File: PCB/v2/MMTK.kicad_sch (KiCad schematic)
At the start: 9 parts

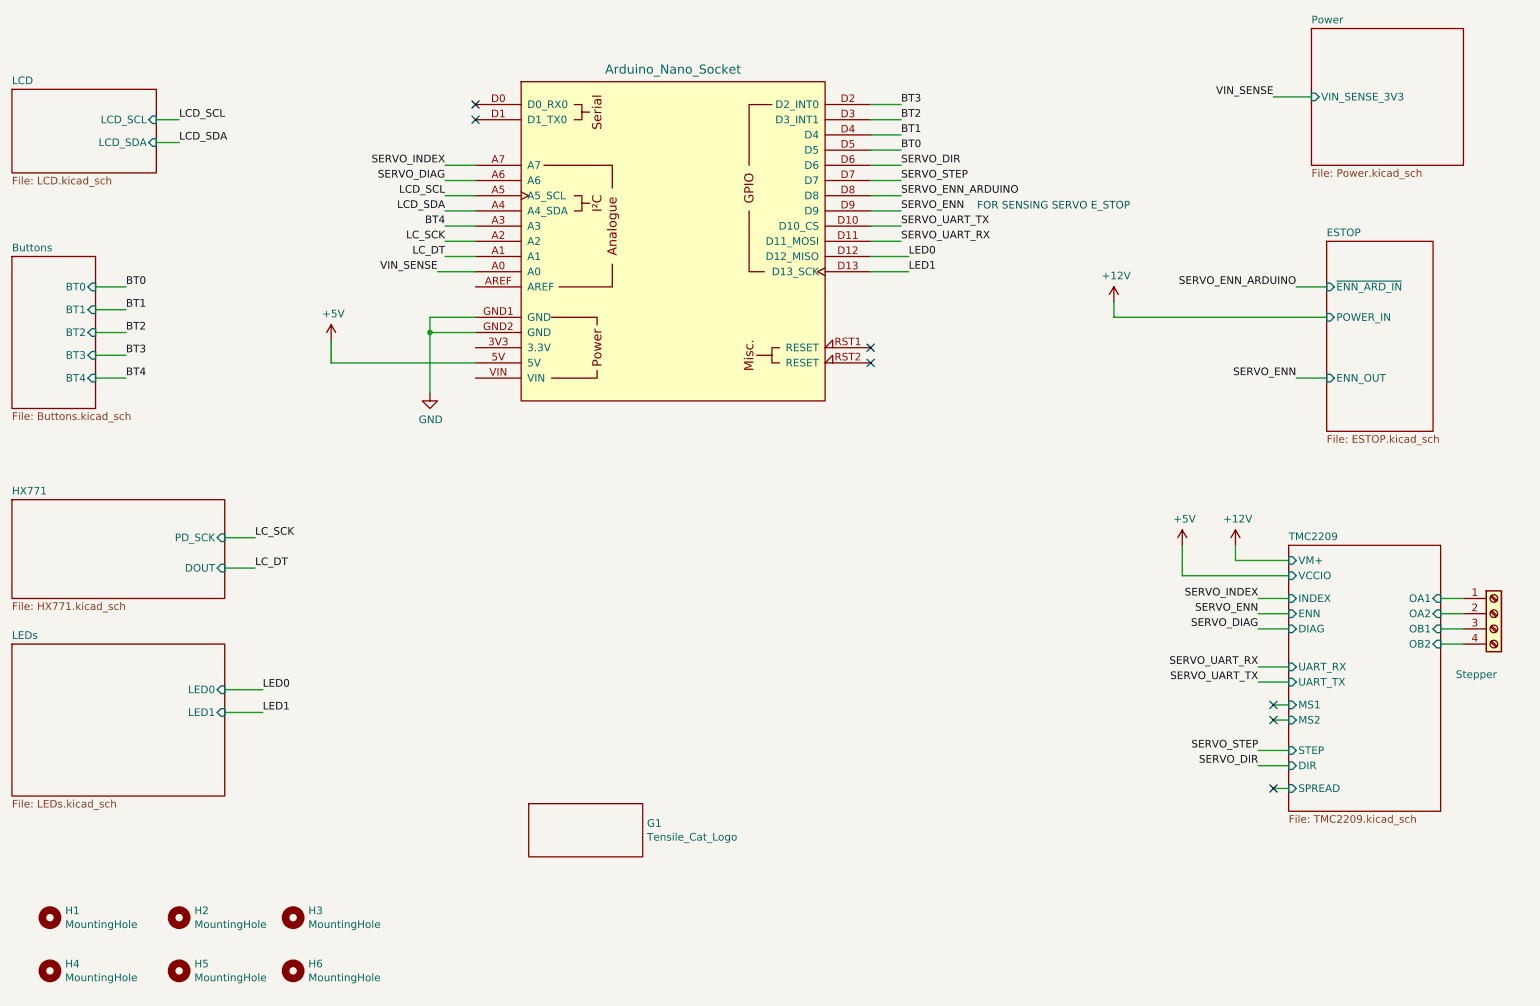
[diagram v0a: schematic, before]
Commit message: WIP updated symbols for tmc5106
Updated footprint for tmc5106,
need to check how motor wiring is done, might be wired up stupid before and that's gonna be sad
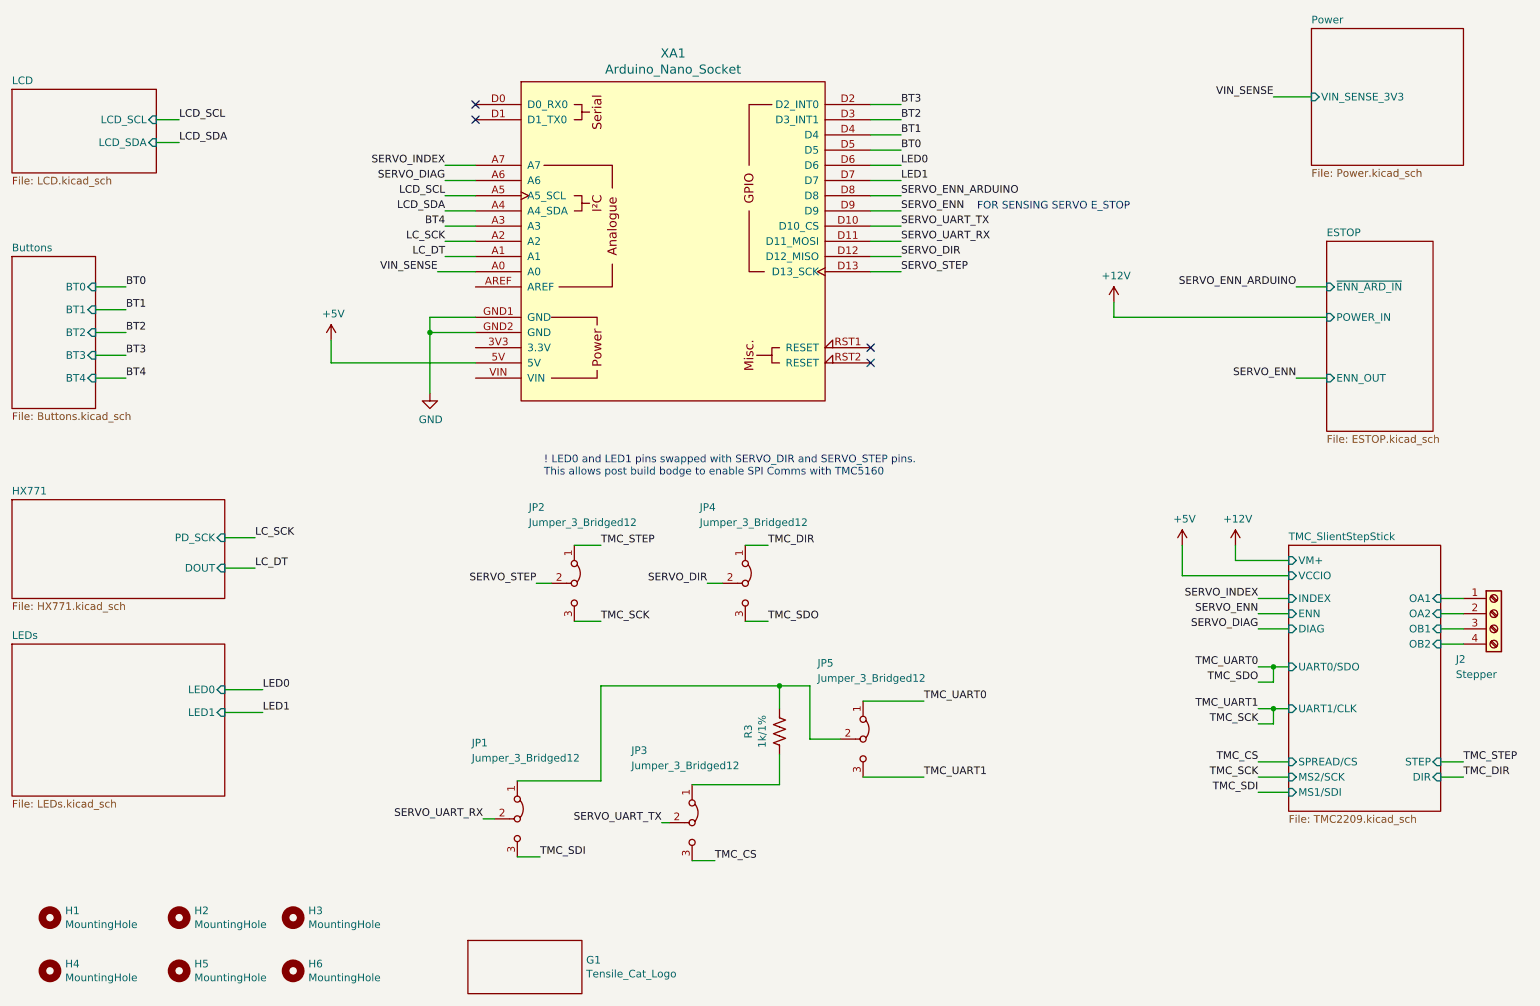
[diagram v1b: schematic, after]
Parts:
- added JP1, JP2, JP3, JP4, JP5: Jumper_3_Bridged12, Jumper:SolderJumper-3_P1.3mm_Bridged12_Pad1.0x1.5mm_NumberLabels, symbol Jumper:Jumper_3_Bridged12
- added R3: 1k/1%, Resistor_SMD:R_0603_1608Metric, symbol MMTK-rescue:R_US-Device-MMTK-rescue-MMTK-rescue
- gave numbers to parts that had none: 2
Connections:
- net LED0: now also XA1.D6; no longer XA1.D12 (D12_MISO)
- net LED1: now also XA1.D7; no longer XA1.D13 (D13_SCK)
- net SERVO_DIR: now also XA1.D12 (D12_MISO), JP4.2 (C); no longer XA1.D6
- net SERVO_STEP: now also XA1.D13 (D13_SCK), JP2.2 (C); no longer XA1.D7
- net SERVO_UART_RX: now also JP1.2 (C)
- net SERVO_UART_TX: now also JP3.2 (C)
- new net: JP1.1 (A), JP5.2 (C), R3.1
- new net: JP3.1 (A), R3.2
- new net TMC_CS: JP3.3 (B)
- new net TMC_DIR: JP4.1 (A)
- new net TMC_SCK: JP2.3 (B), JP5.3 (B)
- new net TMC_SDI: JP1.3 (B)
- new net TMC_SDO: JP4.3 (B), JP5.1 (A)
- new net TMC_STEP: JP2.1 (A)
- no-connect marks 7 -> 4
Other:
- sheet TMC2209 renamed TMC_SlientStepStick
- sheet TMC_SlientStepStick ports: added MS1/SDI, MS2/SCK, SPREAD/CS, UART0/SDO, UART1/CLK; removed MS1, MS2, SPREAD, UART_RX, UART_TX
- note added: "! LED0 and LED1 pins swapped with SERVO_DIR and SERVO_STEP pins. This allows post build bodge to enable SPI Comms with TMC5160"
- moved on the sheet: G1

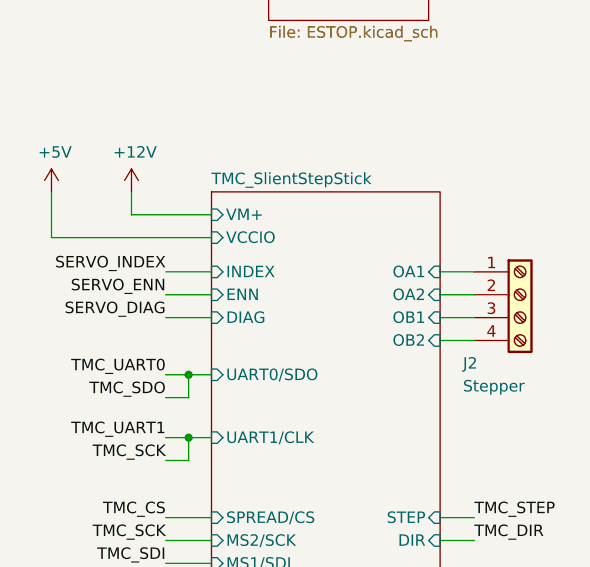
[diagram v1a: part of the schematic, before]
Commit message: Figured Out Motor Wiring
Updated motor wiring, naming on slient step stick is the same as tmc chips itself.
Phrases are A and B and 1/2 are the wires from the same phrase.
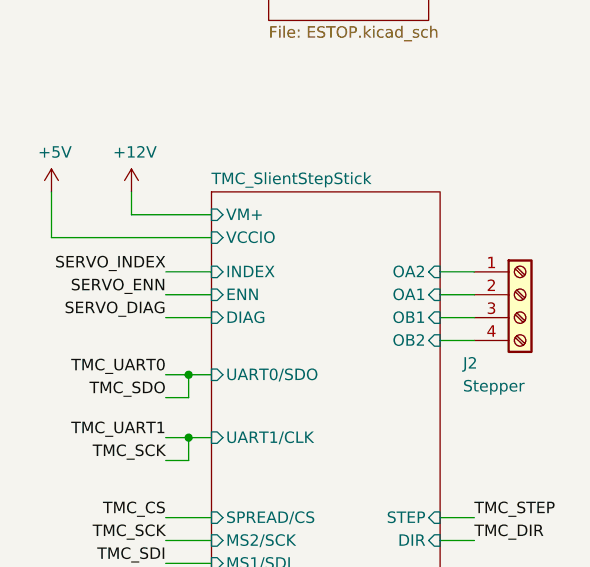
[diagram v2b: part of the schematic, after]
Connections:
- net TMC_SlientStepStick/OA1: now also J2.2 (Pin_2); no longer J2.1 (Pin_1)
- net TMC_SlientStepStick/OA2: now also J2.1 (Pin_1); no longer J2.2 (Pin_2)
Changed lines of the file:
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@@
       (effects (font (size 1.27 1.27)) (justify right))
     )
-    (pin "OA1" input (at 262.89 123.19 0)
+    (pin "OA1" input (at 262.89 125.73 0)
       (effects (font (size 1.27 1.27)) (justify right))
     )
-    (pin "OA2" input (at 262.89 125.73 0)
+    (pin "OA2" input (at 262.89 123.19 0)
       (effects (font (size 1.27 1.27)) (justify right))
     )
